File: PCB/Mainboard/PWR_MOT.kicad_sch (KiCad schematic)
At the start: 36 parts, among them U10 TPS56637RPAR, U8 TPS56637RPAR, U9 TPS56637RPAR

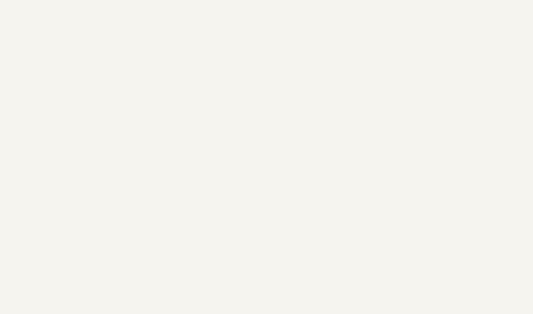
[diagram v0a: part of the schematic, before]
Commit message: Added setup, read and get Command
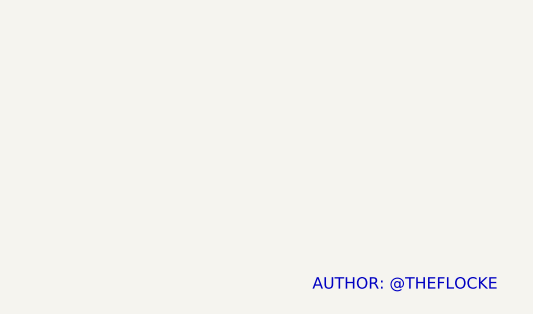
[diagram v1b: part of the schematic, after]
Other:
- note added: "AUTHOR: @THEFLOCKE"
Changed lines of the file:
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@@
 	(generator_version "9.0")
 	(paper "A4")
+	(text "AUTHOR: @THEFLOCKE"
+		(exclude_from_sim no)
+		(at 249.936 196.596 0)
+		(effects
+			(font
+				(face "KiCad Font")
+				(size 1.27 1.27)
+				(color 194 0 194 1)
+			)
+		)
+	)
 	(text "5V 6A"
 		(exclude_from_sim no)
